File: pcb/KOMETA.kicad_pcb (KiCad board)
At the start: 2 copper layers, 279.2 x 87.1 mm, 135 parts

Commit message: update footprint
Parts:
- D1, D10, D11, D12, D13, D14, D15, D16, D17, D18, D19, D2, D20, D21, D22, D23, D24, D25, D26, D27, D28, D29, D3, D30, D31, D32, D33, D34, D35, D36, D37, D38, D39, D4, D40, D41, D42, D5, D6, D7, D8, D9: footprint kometa:Diode -> lib:Diode
- H1, H10, H11, H12, H2, H3, H4, H5, H6, H7, H8, H9: footprint kometa:M2 Hole -> lib:M2 Hole
- KeyChainHole1: footprint kometa:M5 hole -> lib:M5 hole
- PS_L1, PS_R1: footprint kometa:MSK-12C02 -> lib:MSK-12C02
- PW_L1, PW_R1: footprint kometa:Battery -> lib:Battery
- R_L1, R_R1: footprint kometa:Reset -> lib:Reset
- SM_L1, SM_R1: footprint kometa:SuperMini -> lib:SuperMini
- SW1, SW10, SW11, SW12, SW13, SW14, SW15, SW16, SW17, SW18, SW19, SW2, SW20, SW21, SW22, SW23, SW24, SW25, SW26, SW27, SW28, SW29, SW3, SW30, SW31, SW32, SW33, SW34, SW35, SW36, SW37, SW38, SW39, SW4, SW40, SW41, SW42, SW5, SW6, SW7, SW8, SW9: footprint kometa:ChocV2 -> lib:ChocV2
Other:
- board text added: "Case: torowb & customkey"
- board text removed: "Case: toworb & customkey"

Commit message: fix silkscreen
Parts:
- moved G*** 1.00 mm to (336.9, 141.0)
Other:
- board text added: "Case: rowb & customkey"
- board text removed: "Case: torowb & customkey"

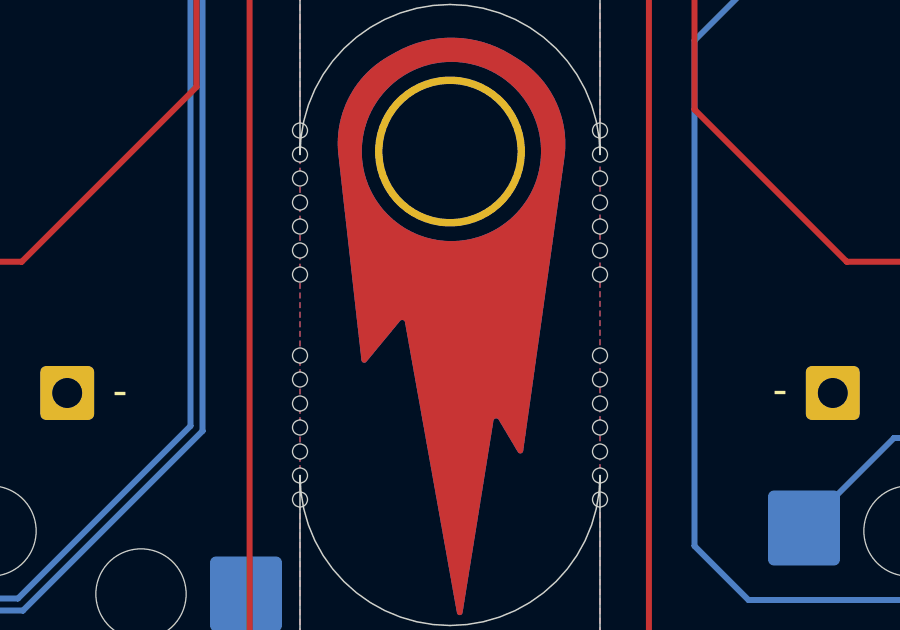
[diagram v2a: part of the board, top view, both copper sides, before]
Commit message: fix EdgeCuts
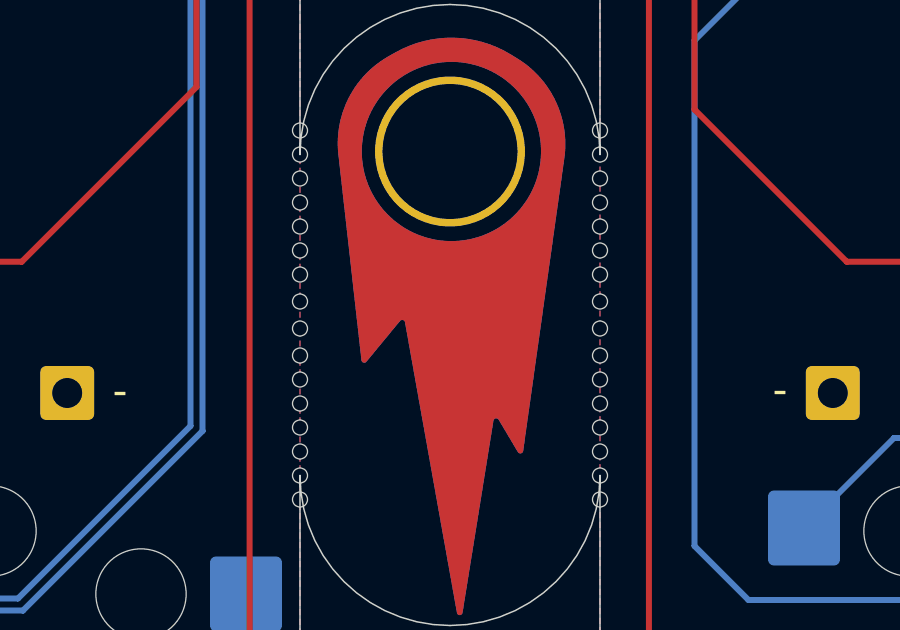
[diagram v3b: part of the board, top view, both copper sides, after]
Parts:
- added ?: , , F.Cu at (212.3, 171.6)
- added ?: , , F.Cu at (212.3, 170.7)
- added ?: , , F.Cu at (202.3, 170.7)
- added ?: , , F.Cu at (202.3, 171.6)
